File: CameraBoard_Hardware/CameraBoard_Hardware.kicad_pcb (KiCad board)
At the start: 2 copper layers, 61 x 99.3 mm, 38 parts, among them J1 BNC_75_OHM_HORIZ, J2 BNC_75_OHM_HORIZ, U1 TM4C129E_Launchpad, U2 OKI, U3 MAX4314ESD+, U4 MAX4314ESD+

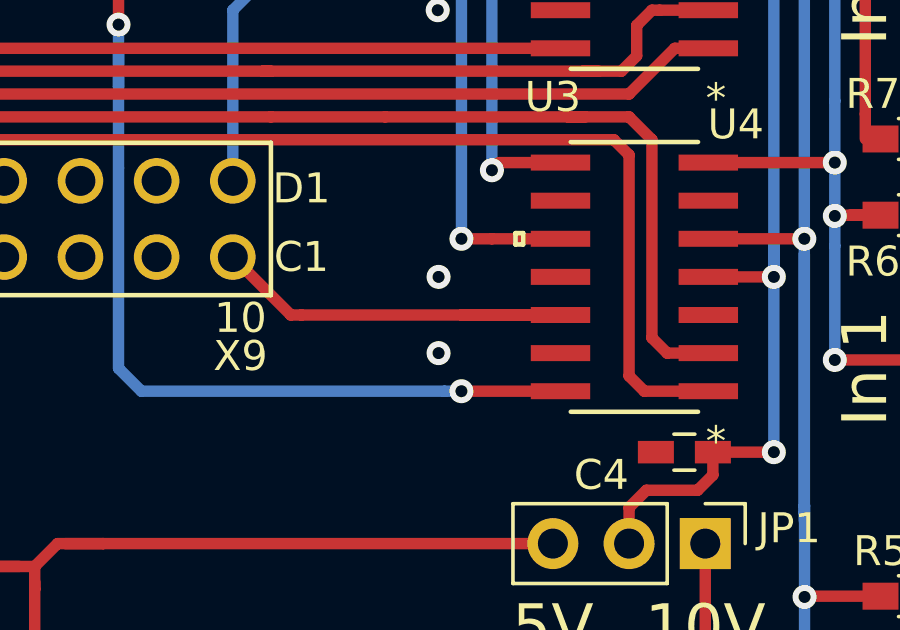
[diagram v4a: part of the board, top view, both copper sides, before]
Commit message: fixed 5V via issue
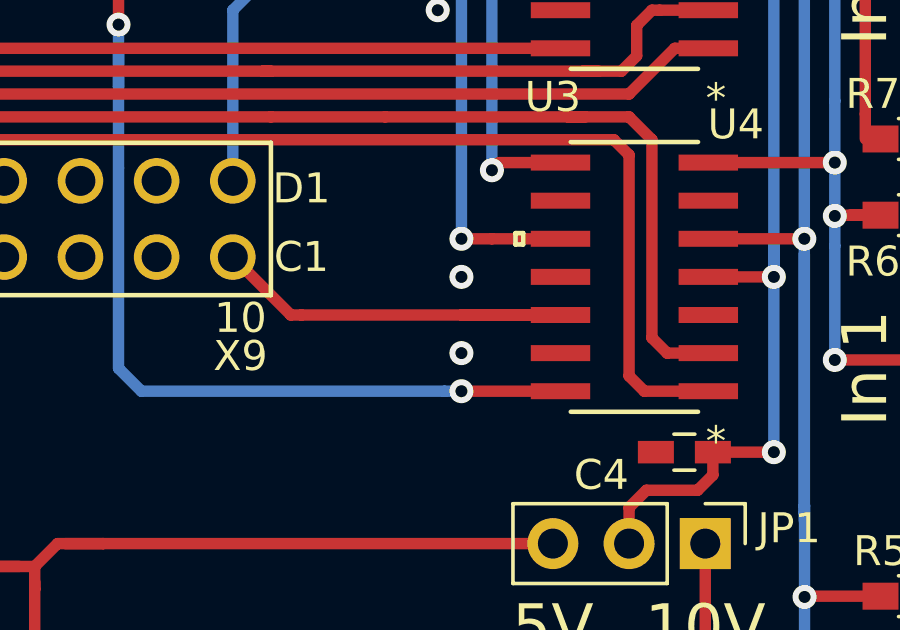
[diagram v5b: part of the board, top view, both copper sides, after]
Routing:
- net GND: vias 6 -> 13
- net +5V: vias 7 -> 0
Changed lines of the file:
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@@
   )
   (setup
-    (last_trace_width 0.381)
+    (last_trace_width 0.25)
     (user_trace_width 0.254)
     (user_trace_width 0.381)
@@
   (via (at 87.628106 107.397) (size 0.8) (drill 0.4) (layers F.Cu B.Cu) (net 2))
   (via (at 92.71 107.442) (size 0.8) (drill 0.4) (layers F.Cu B.Cu) (net 2))
-  (via (at 117.348 88.9) (size 0.8) (drill 0.4) (layers F.Cu B.Cu) (net 21))
-  (via (at 117.3195 77.47) (size 0.8) (drill 0.4) (layers F.Cu B.Cu) (net 21))
-  (via (at 117.3195 74.93) (size 0.8) (drill 0.4) (layers F.Cu B.Cu) (net 21))
-  (via (at 134.366 70.866) (size 0.8) (drill 0.4) (layers F.Cu B.Cu) (net 21))
-  (via (at 134.28 83.058) (size 0.8) (drill 0.4) (layers F.Cu B.Cu) (net 21))
-  (via (at 134.366 94.996) (size 0.8) (drill 0.4) (layers F.Cu B.Cu) (net 21))
-  (via (at 117.348 86.36) (size 0.8) (drill 0.4) (layers F.Cu B.Cu) (net 21))
   (via (at 129.54 85.09) (size 0.8) (drill 0.4) (layers F.Cu B.Cu) (net 3))
   (segment (start 126.3396 85.09) (end 129.54 85.09) (width 0.381) (layer F.Cu) (net 3))
@@
   (segment (start 111.76 76.2) (end 110.49 77.47) (width 0.381) (layer B.Cu) (net 20))
   (segment (start 110.49 77.47) (end 110.49 83.158601) (width 0.381) (layer B.Cu) (net 20))
+  (via (at 118.11 88.9) (size 0.8) (drill 0.4) (layers F.Cu B.Cu) (net 2))
+  (via (at 117.3195 77.47) (size 0.8) (drill 0.4) (layers F.Cu B.Cu) (net 2))
+  (via (at 117.3195 74.93) (size 0.8) (drill 0.4) (layers F.Cu B.Cu) (net 2))
+  (via (at 134.366 70.866) (size 0.8) (drill 0.4) (layers F.Cu B.Cu) (net 2))
+  (via (at 134.28 83.058) (size 0.8) (drill 0.4) (layers F.Cu B.Cu) (net 2))
+  (via (at 134.366 94.996) (size 0.8) (drill 0.4) (layers F.Cu B.Cu) (net 2))
+  (via (at 118.11 86.36) (size 0.8) (drill 0.4) (layers F.Cu B.Cu) (net 2))
   (segment (start 106.172 95.25) (end 104.648 95.25) (width 0.381) (layer F.Cu) (net 21))
   (segment (start 106.172 95.25) (end 104.902 95.25) (width 0.381) (layer F.Cu) (net 21))

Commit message: PRR finish
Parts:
- moved R9 1.36 mm to (91.4, 75.3)
- moved R10 0.09 mm to (106.7, 75.3)
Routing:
- net CAM_OUT0: track 34.8 -> 36.2 mm
- net Net-(J1-Pad2): track 5.09 -> 3.73 mm
- net CAM_OUT1: track 29.0 -> 29.9 mm
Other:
- board text added: "-"
- board text removed: "G"
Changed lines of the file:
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@@
   (general
     (thickness 1.6)
-    (drawings 56)
-    (tracks 248)
+    (drawings 55)
+    (tracks 249)
     (zones 0)
     (modules 38)
@@
   )
   (setup
-    (last_trace_width 0.25)
+    (last_trace_width 0.381)
     (user_trace_width 0.254)
     (user_trace_width 0.381)
@@
     (tags "LED 0603")
     (attr smd)
-    (fp_text reference D1 (at -1.186 3.811894 90) (layer F.SilkS)
+    (fp_text reference D1 (at -1.186 -1.268106 90) (layer F.SilkS)
       (effects (font (size 1 1) (thickness 0.15)))
     )
@@
     (tags "LED 0603")
     (attr smd)
-    (fp_text reference D2 (at 0.084 1.27 90) (layer F.SilkS)
+    (fp_text reference D2 (at 0.846 1.27 90) (layer F.SilkS)
       (effects (font (size 1 1) (thickness 0.15)))
     )
@@
     (tags "LED 0603")
     (attr smd)
-    (fp_text reference D3 (at -1.186 3.81 90) (layer F.SilkS)
+    (fp_text reference D3 (at 1.1 -1.27 90) (layer F.SilkS)
       (effects (font (size 1 1) (thickness 0.15)))
     )
@@
     (tags "LED 0603")
     (attr smd)
-    (fp_text reference D4 (at 1.354 1.27 90) (layer F.SilkS)
+    (fp_text reference D4 (at -1.186 1.27 90) (layer F.SilkS)
       (effects (font (size 1 1) (thickness 0.15)))
     )
@@
   )
   (module Resistors_SMD:R_0603_HandSoldering (layer F.Cu)
-    (at 91.44 76.624 90)
+    (at 91.44 75.268 90)
     (descr "Resistor SMD 0603, hand soldering")
     (tags "resistor 0603")
@@
   )
   (module Resistors_SMD:R_0603_HandSoldering (layer F.Cu)
-    (at 106.68 75.354 90)
+    (at 106.68 75.268 90)
     (descr "Resistor SMD 0603, hand soldering")
     (tags "resistor 0603")
@@
     (tags "LED 0603")
     (attr smd)
-    (fp_text reference D6 (at 1.354 1.27 90) (layer F.SilkS)
+    (fp_text reference D6 (at -1.186 1.27 90) (layer F.SilkS)
       (effects (font (size 1 1) (thickness 0.15)))
     )
@@
     (tags "LED 0603")
     (attr smd)
-    (fp_text reference D7 (at 0.084 1.524 90) (layer F.SilkS)
+    (fp_text reference D7 (at 1.1 -1.27 90) (layer F.SilkS)
       (effects (font (size 1 1) (thickness 0.15)))
     )
@@
       (net 21 +5V))
   )
-  (gr_text 5V (at 97.409 111.379) (layer F.SilkS)
-    (effects (font (size 1.5 1.5) (thickness 0.3)))
-  )
-  (gr_text G (at 131.826 99.568) (layer B.SilkS)
+  (gr_line (start 101.6 89.154) (end 86.36 89.154) (layer F.SilkS) (width 0.2))
+  (gr_line (start 101.6 106.68) (end 86.36 106.68) (layer F.SilkS) (width 0.2))
+  (gr_line (start 101.6 106.68) (end 101.6 89.154) (layer F.SilkS) (width 0.2))
+  (gr_text - (at 131.826 61.468) (layer B.SilkS)
     (effects (font (size 1.5 1.5) (thickness 0.3)) (justify mirror))
   )
-  (gr_text +12 (at 130.302 104.648) (layer B.SilkS)
+  (gr_text S (at 131.826 64.008) (layer B.SilkS)
     (effects (font (size 1.5 1.5) (thickness 0.3)) (justify mirror))
   )
-  (gr_text S (at 131.826 102.108) (layer B.SilkS)
+  (gr_text +12 (at 130.302 66.548) (layer B.SilkS)
     (effects (font (size 1.5 1.5) (thickness 0.3)) (justify mirror))
   )
-  (gr_text S (at 132.08 89.408) (layer B.SilkS)
+  (gr_text - (at 131.826 74.168) (layer B.SilkS)
     (effects (font (size 1.5 1.5) (thickness 0.3)) (justify mirror))
   )
-  (gr_text G (at 132.08 86.868) (layer B.SilkS)
+  (gr_text +12 (at 130.302 79.248) (layer B.SilkS)
     (effects (font (size 1.5 1.5) (thickness 0.3)) (justify mirror))
   )
-  (gr_text +12 (at 130.556 91.948) (layer B.SilkS)
+  (gr_text S (at 131.826 76.708) (layer B.SilkS)
     (effects (font (size 1.5 1.5) (thickness 0.3)) (justify mirror))
   )
-  (gr_text +12 (at 130.556 79.248) (layer B.SilkS)
+  (gr_text - (at 131.826 86.868) (layer B.SilkS)
     (effects (font (size 1.5 1.5) (thickness 0.3)) (justify mirror))
   )
-  (gr_text S (at 132.08 76.708) (layer B.SilkS)
+  (gr_text +12 (at 130.302 91.948) (layer B.SilkS)
     (effects (font (size 1.5 1.5) (thickness 0.3)) (justify mirror))
   )
-  (gr_text G (at 132.08 74.168) (layer B.SilkS)
+  (gr_text S (at 131.826 89.408) (layer B.SilkS)
     (effects (font (size 1.5 1.5) (thickness 0.3)) (justify mirror))
   )
-  (gr_text +12 (at 130.556 66.548) (layer B.SilkS)
+  (gr_text 5V (at 97.409 111.379) (layer F.SilkS)
+    (effects (font (size 1.5 1.5) (thickness 0.3)))
+  )
+  (gr_text - (at 131.826 99.568) (layer B.SilkS)
     (effects (font (size 1.5 1.5) (thickness 0.3)) (justify mirror))
   )
-  (gr_text S (at 132.08 64.008) (layer B.SilkS)
+  (gr_text +12 (at 130.302 104.648) (layer B.SilkS)
     (effects (font (size 1.5 1.5) (thickness 0.3)) (justify mirror))
   )
-  (gr_text G (at 132.08 61.468) (layer B.SilkS)
+  (gr_text S (at 131.826 102.108) (layer B.SilkS)
     (effects (font (size 1.5 1.5) (thickness 0.3)) (justify mirror))
   )
   (gr_line (start 96.52 89.154) (end 96.52 106.68) (layer F.SilkS) (width 0.2))
   (gr_line (start 91.44 89.154) (end 91.44 106.68) (layer F.SilkS) (width 0.2))
-  (gr_line (start 102.362 89.154) (end 86.36 89.154) (layer F.SilkS) (width 0.2))
-  (gr_line (start 102.362 95.758) (end 102.362 89.154) (layer F.SilkS) (width 0.2))
-  (gr_line (start 102.362 106.68) (end 102.362 95.758) (layer F.SilkS) (width 0.2))
-  (gr_line (start 86.36 106.68) (end 102.362 106.68) (layer F.SilkS) (width 0.2))
   (gr_text 5V (at 121.158 98.044) (layer F.SilkS)
     (effects (font (size 1.5 1.5) (thickness 0.3)))
@@
   (segment (start 131.572 63.9826) (end 134.112 63.9826) (width 0.381) (layer F.Cu) (net 6))
   (segment (start 131.572 64.4906) (end 132.08 63.9826) (width 0.381) (layer F.Cu) (net 6))
-  (segment (start 131.607 68.8086) (end 131.572 68.7736) (width 0.381) (layer F.Cu) (net 6))
   (segment (start 131.572 68.5546) (end 131.572 64.4906) (width 0.381) (layer F.Cu) (net 6))
   (segment (start 132.08 69.0626) (end 131.572 68.5546) (width 0.381) (layer F.Cu) (net 6))
@@
   (segment (start 92.71 85.698601) (end 92.71 86.773403) (width 0.381) (layer F.Cu) (net 13))
   (segment (start 92.71 98.212) (end 92.71 100.584) (width 0.381) (layer F.Cu) (net 14))
-  (segment (start 91.44 70.4342) (end 91.44 75.524) (width 0.381) (layer F.Cu) (net 15))
-  (segment (start 106.68 74.254) (end 106.68 70.4342) (width 0.381) (layer F.Cu) (net 16))
   (segment (start 100.076 78.74) (end 95.758 78.74) (width 0.381) (layer F.Cu) (net 17))
   (segment (start 121.412 78.74) (end 100.076 78.74) (width 0.381) (layer F.Cu) (net 17))
-  (segment (start 91.44 77.874) (end 91.44 77.724) (width 0.381) (layer F.Cu) (net 17))
-  (segment (start 92.306 78.74) (end 91.44 77.874) (width 0.381) (layer F.Cu) (net 17))
-  (segment (start 100.076 78.74) (end 92.306 78.74) (width 0.381) (layer F.Cu) (net 17))
   (via (at 118.11 90.17) (size 0.8) (drill 0.4) (layers F.Cu B.Cu) (net 18))
   (segment (start 121.412 90.17) (end 118.11 90.17) (width 0.381) (layer F.Cu) (net 18))
@@
   (segment (start 106.68 80.01) (end 106.68 78.74) (width 0.381) (layer B.Cu) (net 18))
   (segment (start 106.68 82.725859) (end 106.68 80.01) (width 0.381) (layer B.Cu) (net 18))
-  (segment (start 106.68 77.9495) (end 106.68 76.708) (width 0.381) (layer F.Cu) (net 18))
   (segment (start 121.412 87.63) (end 120.0404 87.63) (width 0.381) (layer F.Cu) (net 19))
   (segment (start 121.412 87.63) (end 118.11 87.63) (width 0.381) (layer F.Cu) (net 19))
@@
   (segment (start 111.76 76.2) (end 110.49 77.47) (width 0.381) (layer B.Cu) (net 20))
   (segment (start 110.49 77.47) (end 110.49 83.158601) (width 0.381) (layer B.Cu) (net 20))
-  (via (at 118.11 88.9) (size 0.8) (drill 0.4) (layers F.Cu B.Cu) (net 2))
-  (via (at 117.3195 77.47) (size 0.8) (drill 0.4) (layers F.Cu B.Cu) (net 2))
-  (via (at 117.3195 74.93) (size 0.8) (drill 0.4) (layers F.Cu B.Cu) (net 2))
+  (via (at 116.84 88.9) (size 0.8) (drill 0.4) (layers F.Cu B.Cu) (net 2))
+  (via (at 116.078 77.47) (size 0.8) (drill 0.4) (layers F.Cu B.Cu) (net 2))
+  (via (at 116.078 74.93) (size 0.8) (drill 0.4) (layers F.Cu B.Cu) (net 2))
   (via (at 134.366 70.866) (size 0.8) (drill 0.4) (layers F.Cu B.Cu) (net 2))
   (via (at 134.28 83.058) (size 0.8) (drill 0.4) (layers F.Cu B.Cu) (net 2))
   (via (at 134.366 94.996) (size 0.8) (drill 0.4) (layers F.Cu B.Cu) (net 2))
-  (via (at 118.11 86.36) (size 0.8) (drill 0.4) (layers F.Cu B.Cu) (net 2))
+  (via (at 116.84 86.36) (size 0.8) (drill 0.4) (layers F.Cu B.Cu) (net 2))
+  (segment (start 91.44 70.4342) (end 91.44 74.168) (width 0.381) (layer F.Cu) (net 15))
+  (segment (start 106.68 70.4342) (end 106.68 74.168) (width 0.381) (layer F.Cu) (net 16))
+  (segment (start 92.306 78.74) (end 100.076 78.74) (width 0.381) (layer F.Cu) (net 17))
+  (segment (start 91.44 76.368) (end 91.44 77.874) (width 0.381) (layer F.Cu) (net 17))
+  (segment (start 91.44 77.874) (end 92.306 78.74) (width 0.381) (layer F.Cu) (net 17))
+  (segment (start 106.68 76.368) (end 106.68 77.216) (width 0.381) (layer F.Cu) (net 18))
+  (segment (start 106.68 77.9495) (end 106.68 77.216) (width 0.381) (layer F.Cu) (net 18))
+  (segment (start 106.68 77.216) (end 106.68 76.708) (width 0.381) (layer F.Cu) (net 18))
   (segment (start 106.172 95.25) (end 104.648 95.25) (width 0.381) (layer F.Cu) (net 21))
   (segment (start 106.172 95.25) (end 104.902 95.25) (width 0.381) (layer F.Cu) (net 21))
